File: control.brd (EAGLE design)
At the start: 139.5 x 34.5 mm, 65 parts, among them IC3 ATTINY85-20S

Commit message: completes first ideration
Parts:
- removed U$43: 2N7002P, LED Driver:SOT23
- added SL2: (no value), con-amp-quick:07P
- added U$38: 2N7002P, Smile_Shade:SOT23
- U$10, U$12, U$14, U$16, U$18, U$20, U$22, U$24, U$26, U$28, U$30, U$32, U$34, U$4, U$41, U$6, U$8: device LED Driver:SOT23 -> Smile_Shade:SOT23
- moved R8 92.8 mm to (150.5, 16.5), turned to 180 degrees
- moved U$17 91.2 mm to (149.5, 18.5), turned to 0 degrees
- moved U$4 82.0 mm to (146.0, 12.0), turned to 0 degrees
- moved R1 80.4 mm to (145.0, 16.5), turned to 180 degrees
- moved U$3 78.8 mm to (144.0, 18.5), turned to 0 degrees
- moved U$36 77.6 mm to (59.5, 31.0)
- moved U$6 69.5 mm to (140.5, 12.0), turned to 0 degrees
- moved R2 67.9 mm to (139.5, 16.5), turned to 180 degrees
- moved U$5 66.5 mm to (138.5, 18.5), turned to 0 degrees
- moved U$35 63.7 mm to (73.5, 29.0), turned to 0 degrees
- moved U$8 57.0 mm to (135.0, 12.0), turned to 0 degrees
- moved R3 55.5 mm to (134.0, 16.5), turned to 180 degrees
- moved U$7 54.2 mm to (133.0, 18.5), turned to 0 degrees
- moved U$2 48.4 mm to (97.3, 34.5)
- moved R6 42.9 mm to (128.4, 16.3), turned to 180 degrees
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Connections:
- removed net 24V: U$2.8
- new net +3V3: IC3.8
- new net ENDSTOP0: SL2.3, U$1.CSID0
- new net ENDSTOP1: SL2.4, U$1.CSID1
- new net ENDSTOP2: SL2.5, U$1.CSID2
- new net ENDSTOP3: SL2.6, U$1.CSID3
- net 3V3: now also SL2.7, U$2.16; no longer IC3.8
- net 48V: now also SL2.1
- net 5V: now also U$2.8; no longer U$2.16
- net ENCOUT: now also U$1.UART2-TX; no longer U$1.USB1_N
- net GND: now also SL2.2, U$38.P$1; no longer U$43.P$1
- net LEDSTR_1: now also U$44.P$1; no longer U$44.P$9
- net LEDSTR_11: now also U$44.P$11; no longer U$44.P$1
- net LEDSTR_2: now also U$44.P$2; no longer U$44.P$8
- net LEDSTR_3: now also U$44.P$3; no longer U$44.P$7
- net LEDSTR_4: now also U$44.P$4; no longer U$44.P$6
- net LEDSTR_5: now also U$44.P$7; no longer U$44.P$3
- net LEDSTR_6: now also U$44.P$6; no longer U$44.P$4
- net LEDSTR_8: now also U$44.P$8; no longer U$44.P$2
- net LEDSTR_9: now also U$44.P$9; no longer U$44.P$11
- net N$11: now also U$12.P$3; no longer U$14.P$3
- net N$13: now also U$10.P$3; no longer U$16.P$3
- net N$15: now also U$38.P$3; no longer U$18.P$3
- net N$17: now also U$18.P$3; no longer U$20.P$3
- net N$19: now also U$20.P$3; no longer U$22.P$3
- net N$21: now also U$22.P$3; no longer U$24.P$3
- net N$23: now also U$24.P$3; no longer U$26.P$3
- net N$25: now also U$32.P$3; no longer U$28.P$3
- net N$29: now also U$28.P$3; no longer U$32.P$3
- net N$31: now also U$26.P$3; no longer U$34.P$3
- net N$35: now also U$34.P$3; no longer U$41.P$3
- net N$37: now also U$41.P$3; no longer U$43.P$3
- net N$7: now also U$16.P$3; no longer U$10.P$3
- net N$9: now also U$14.P$3; no longer U$12.P$3
- net ZN0: now also U$38.P$2; no longer U$18.P$2
- net ZN11: now also U$32.P$2; no longer U$28.P$2
- net ZN12: now also U$24.P$2; no longer U$26.P$2
- net ZN13: now also U$18.P$2; no longer U$20.P$2
- net ZN14: now also U$20.P$2; no longer U$22.P$2
- net ZN15: now also U$22.P$2; no longer U$24.P$2
- net ZN16: now also U$41.P$2; no longer U$43.P$2
- net ZN4: now also U$12.P$2; no longer U$14.P$2
- net ZN5: now also U$14.P$2; no longer U$12.P$2
- net ZN6: now also U$16.P$2; no longer U$10.P$2
- net ZN7: now also U$10.P$2; no longer U$16.P$2
- net ZN8: now also U$26.P$2; no longer U$41.P$2
- net ZN9: now also U$28.P$2; no longer U$32.P$2
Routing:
- net 3V3: track 0.00 -> 225.4 mm, vias 0 -> 5
- net ENDSTOP2: track 0.00 -> 212.2 mm, vias 0 -> 3
- net 48V: track 0.00 -> 175.5 mm
- net ENDSTOP1: track 0.00 -> 146.3 mm, vias 0 -> 2
- net ENDSTOP3: track 0.00 -> 144.8 mm, vias 0 -> 4
- net ENDSTOP0: track 0.00 -> 142.6 mm, vias 0 -> 4
- net LEDSTR_12: track 0.00 -> 138.6 mm, vias 0 -> 2
- net M2B: track 0.00 -> 102.2 mm, vias 0 -> 2
- net LEDSTR_17: track 0.00 -> 95.4 mm, vias 0 -> 4
- net M1: track 0.00 -> 95.3 mm, vias 0 -> 4
- net LEDSTR_18: track 0.00 -> 93.6 mm, vias 0 -> 2
- net LEDSTR_16: track 0.00 -> 89.6 mm, vias 0 -> 2
- net M2A: track 0.00 -> 88.0 mm, vias 0 -> 1
- net 5V: track 0.00 -> 86.4 mm, vias 0 -> 2
- net LEDSTR_15: track 0.00 -> 84.3 mm, vias 0 -> 2
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- added copper zone on layer 16, net 48V
- added copper zone on layer 1, net GND
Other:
- board size 139.5 x 34.5 mm -> 156 x 36 mm
- board text added: "2017"
- board text added: "Louis Adamian Patent Pending"
- board text added: "Smile Shade control PCB v1.0"
- board text added: "©"

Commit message: adds actual route
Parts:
- removed SL2: (no value), con-amp-quick:07P
- added SL3: (no value), con-amp-quick:09P
- moved U$37 4.00 mm to (109.5, 3.00)
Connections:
- net 3V3: now also SL3.7; no longer SL2.7
- net 48V: now also SL3.1; no longer SL2.1
- net ENDSTOP0: now also SL3.3; no longer SL2.3
- net ENDSTOP1: now also SL3.4; no longer SL2.4
- net ENDSTOP2: now also SL3.5; no longer SL2.5
- net ENDSTOP3: now also SL3.6; no longer SL2.6
- net GND: now also SL3.2; no longer SL2.2
- net M1A: now also SL3.8
- net M1B: now also SL3.9
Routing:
- net GND: track 13.8 -> 352.8 mm, vias 1 -> 3
- net M1A: track 0.00 -> 108.5 mm
- net M1B: track 0.00 -> 78.6 mm, vias 0 -> 1
- net LEDSTR_12: track 138.6 -> 63.3 mm
- net ENDSTOP2: track 212.2 -> 137.6 mm, vias 3 -> 6
- net 5V: track 86.4 -> 125.6 mm, vias 2 -> 1
- net 48V: track 175.5 -> 208.0 mm, vias 0 -> 3
- net 3V3: track 225.4 -> 252.4 mm
- net ZN1: track 42.8 -> 65.0 mm
- net ENDSTOP3: track 144.8 -> 130.1 mm, vias 4 -> 3
- net ENDSTOP1: track 146.3 -> 132.5 mm, vias 2 -> 3
- net ENDSTOP0: track 142.6 -> 130.2 mm, vias 4 -> 5
- net LEDSTR_4: track 34.3 -> 23.3 mm
- net N$34: track 64.4 -> 54.0 mm, vias 0 -> 1
- net ZN3: track 35.2 -> 25.3 mm
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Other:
- board size 156 x 36 mm -> 156 x 38 mm

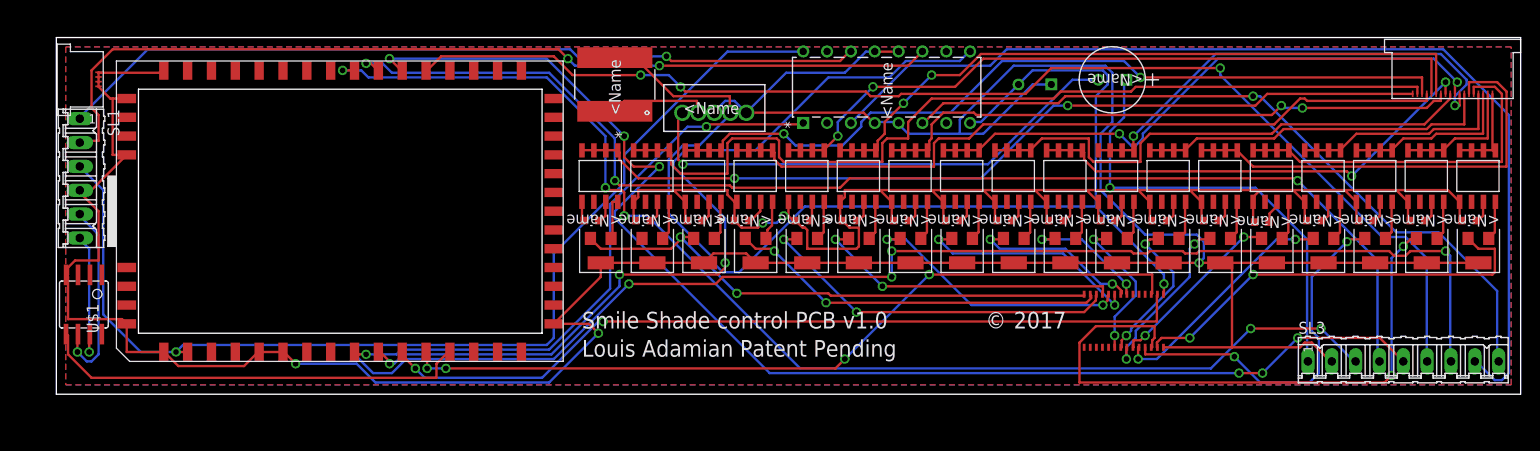
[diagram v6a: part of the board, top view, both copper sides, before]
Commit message: fixes DRC err
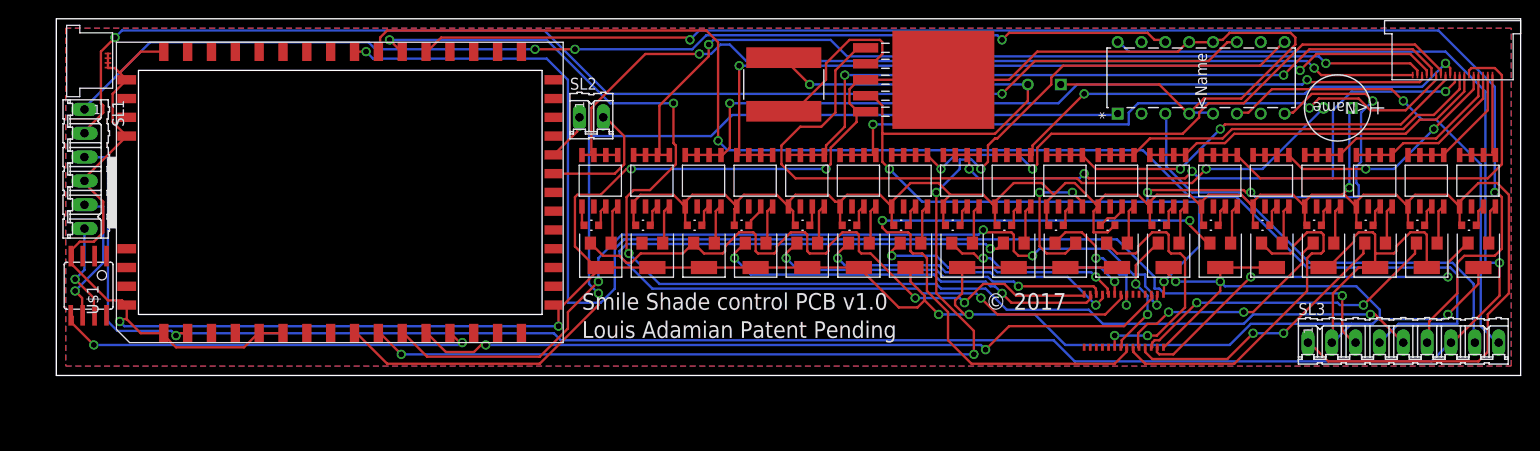
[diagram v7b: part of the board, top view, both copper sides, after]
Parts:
- removed R18: RC0603FR-0710RL, LED Driver:RC0603N
- removed U$35: LM2576HVT-5.0/NOPB, LED Driver:T05A
- added R19: RC0603FR-0710RL, Smile_Shade:RC0603N
- added SL2: (no value), con-amp-quick:02P
- added U$43: LM2576HVSX-5.0/NOPB, Smile_Shade:TS5B
- R1, R10, R11, R12, R13, R14, R15, R16, R17, R2, R3, R4, R5, R6, R7, R8, R9: device LED Driver:RC0603N -> Smile_Shade:RC0603N
- moved U$2 33.5 mm to (130.8, 35.5)
- moved C2 24.2 mm to (135.0, 28.5)
- moved R12 22.0 mm to (68.0, 16.0)
- moved U$36 18.0 mm to (77.5, 31.0)
- moved R11 16.5 mm to (90.0, 16.0)
- moved R3 16.5 mm to (117.5, 16.0)
- moved R7 16.5 mm to (95.5, 16.0)
- moved R6 16.4 mm to (112.0, 16.0), turned to 0 degrees
- moved R13 11.5 mm to (73.0, 16.0)
- moved R15 11.5 mm to (84.5, 16.0)
- moved R16 11.0 mm to (57.0, 16.0)
- moved R1 5.52 mm to (139.5, 16.0)
- moved R10 5.52 mm to (106.5, 16.0)
- moved R17 5.52 mm to (62.5, 16.0)
- moved R2 5.52 mm to (134.0, 16.0)
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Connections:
- new net N$39: SL2.1, U$1.I2S+SPDIF
- new net N$40: SL2.2, U$1.I2S-DO
- net 48: now also R16.2; no longer R17.2
- net 48V: now also R17.2, R19.2; no longer R16.2, R18.2
- net 5V: now also U$43.4; no longer U$35.4
- net GND: now also U$43.3, U$43.5, U$43.6; no longer U$35.3, U$35.5
- net N$10: now also R4.1; no longer R5.1
- net N$12: now also R5.1; no longer R6.1
- net N$14: now also R6.1; no longer R7.1
- net N$18: now also R7.1; no longer R9.1
- net N$2: now also R19.1; no longer R1.1
- net N$20: now also R9.1; no longer R10.1
- net N$22: now also R10.1; no longer R11.1
- net N$24: now also R11.1; no longer R12.1
- net N$26: now also R15.1; no longer R13.1
- net N$30: now also R13.1; no longer R15.1
- net N$32: now also R12.1; no longer R16.1
- net N$33: now also U$43.2; no longer U$35.2
- net N$34: now also U$43.1; no longer U$35.1
- net N$36: now also R16.1; no longer R17.1
- net N$38: now also R17.1; no longer R18.1
- net N$4: now also R1.1; no longer R2.1
- net N$6: now also R2.1; no longer R3.1
- net N$8: now also R3.1; no longer R4.1
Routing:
- net GND: track 352.8 -> 458.6 mm, vias 3 -> 9
- net ZN14: track 18.1 -> 99.4 mm
- net M1A: track 108.5 -> 50.0 mm
- net ZN5: track 18.4 -> 74.9 mm
- net M0: track 63.4 -> 105.7 mm, vias 2 -> 1
- net M1: track 92.6 -> 129.9 mm, vias 3 -> 4
- net M2B: track 100.8 -> 136.7 mm
- net M2A: track 86.2 -> 120.1 mm, vias 1 -> 3
- net ZN1: track 65.0 -> 33.9 mm
- net M1B: track 78.6 -> 50.2 mm
- net N$34: track 54.0 -> 79.8 mm
- net 5V: track 125.6 -> 146.7 mm, vias 1 -> 6
- net ENDSTOP3: track 130.1 -> 150.5 mm, vias 3 -> 2
- net ZN4: track 19.1 -> 38.5 mm, vias 2 -> 0
- net ENDSTOP1: track 132.5 -> 148.0 mm, vias 3 -> 1
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- added copper zone on layer 16, net 48VDD
- added copper zone on layer 1, net GNDDD
- removed copper zone on layer 16, net 48V
- removed copper zone on layer 1, net GND

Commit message: adds ADC input with all RDC and  rounting
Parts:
- removed SL2: (no value), con-amp-quick:02P
- added SL4: (no value), con-amp-quick:03P
- moved U$39 1.00 mm to (5.00, 36.5)
- moved SL1 0.50 mm to (2.50, 22.0)
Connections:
- removed net AGND: U$1.AGND
- new net N$41: SL4.1, U$1.MICIN2
- net N$39: now also SL4.3, U$1.AGND; no longer SL2.1, U$1.I2S+SPDIF
- net N$40: now also SL4.2, U$1.MICIN1; no longer SL2.2, U$1.I2S-DO
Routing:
- net GND: track 458.6 -> 305.5 mm, vias 9 -> 5
- net ZN14: track 99.4 -> 14.7 mm
- net ZN5: track 74.9 -> 16.6 mm
- net 48V: track 207.0 -> 175.2 mm
- net M2B: track 136.7 -> 164.1 mm, vias 2 -> 4
- net N$34: track 79.8 -> 104.7 mm
- net LEDSTR_18: track 95.3 -> 119.8 mm
- net 5V: track 146.7 -> 122.3 mm, vias 6 -> 2
- net ENDSTOP1: track 148.0 -> 127.8 mm, vias 1 -> 3
- net M1: track 129.9 -> 112.1 mm
- net SDA: track 96.8 -> 83.0 mm, vias 4 -> 2
- net ZN7: track 27.4 -> 13.8 mm
- net M1A: track 50.0 -> 63.6 mm
- net 3V3: track 239.2 -> 225.7 mm
- net ZN8: track 68.0 -> 55.6 mm
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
